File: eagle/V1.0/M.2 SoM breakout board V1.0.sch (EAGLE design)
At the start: 121 parts, among them J1 3-PIN SMD, J11 WAFER-HY2.0-4PWB, J18 PARTICLE-STUDIOS_M_SERIES_M.2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, J2 DCJ0202, J21 SIP-2, J3 SPARK_CON_30X2_SMD, J5 SCREW-HOLE-3.7, J6 M.2-SOM-BREAKOUT-BOARD-V0.3_M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, J7 SCREW-HOLE-3.7, Q1 DNP/L2N7002, Q2 SI2333DS, Q3 SI2333DS, Q4 SI2333DS, Q5 SI2333DS, U1 XC8107, X1 BU-SMA-G, X2 BU-SMA-G, X3 BU-SMA-G, X4 S8111-46R, X5 S8111-46R, X6 S8111-46R

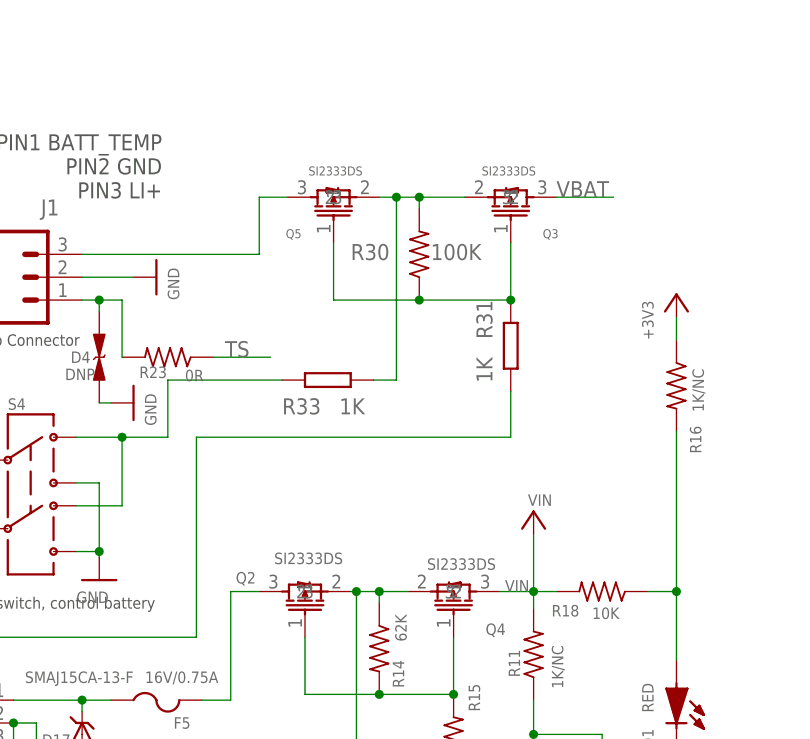
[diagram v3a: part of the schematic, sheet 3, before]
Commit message: Move Q2 position.
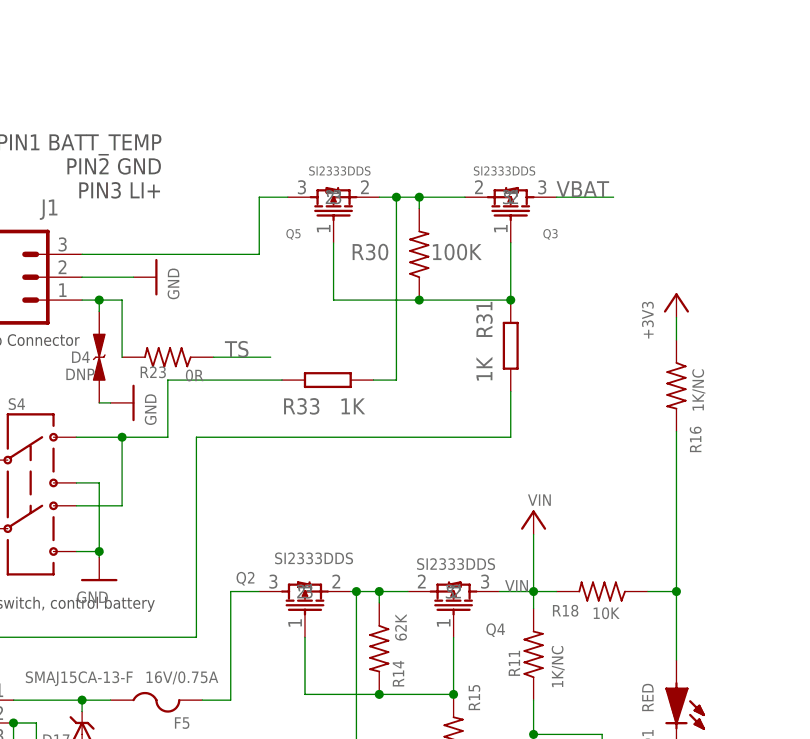
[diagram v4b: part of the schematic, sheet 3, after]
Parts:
- Q2, Q3, Q4, Q5: value SI2333DS -> SI2333DDS
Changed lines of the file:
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@@
 <part name="GND35" library="supply1" library_urn="urn:adsk.eagle:library:371" deviceset="GND" device=""/>
 <part name="S1" library="SparkFun-Retired" deviceset="SWITCH-DPDT" device=""/>
-<part name="Q4" library="RedBear" deviceset="PMOS" device="" value="SI2333DS"/>
+<part name="Q4" library="RedBear" deviceset="PMOS" device="" value="SI2333DDS"/>
 <part name="GND6" library="supply1" library_urn="urn:adsk.eagle:library:371" deviceset="GND" device=""/>
 <part name="R15" library="Particle" deviceset="R-US_" device="" value="36K"/>
@@
 <part name="J21" library="particle SZ" library_urn="urn:adsk.eagle:library:21650216" deviceset="SIP-2" device="" package3d_urn="urn:adsk.eagle:package:21650858/5"/>
 <part name="R30" library="particle-studios" library_urn="urn:adsk.eagle:library:10700396" deviceset="RES_" device="0603" package3d_urn="urn:adsk.eagle:package:10700443/4" technology="100K_" value="100K"/>
-<part name="Q3" library="RedBear" deviceset="PMOS" device="" value="SI2333DS"/>
-<part name="Q5" library="RedBear" deviceset="PMOS" device="" value="SI2333DS"/>
+<part name="Q3" library="RedBear" deviceset="PMOS" device="" value="SI2333DDS"/>
+<part name="Q5" library="RedBear" deviceset="PMOS" device="" value="SI2333DDS"/>
 <part name="R31" library="RedBear" deviceset="RES" device="0402S" value="1K"/>
 <part name="LED3" library="particle SZ" deviceset="LED" device="" value="yellow"/>
@@
 <part name="GND21" library="supply1" library_urn="urn:adsk.eagle:library:371" deviceset="GND" device=""/>
 <part name="D4" library="particle SZ" deviceset="ESD" device="" value="DNP"/>
-<part name="Q2" library="RedBear" deviceset="PMOS" device="" value="SI2333DS"/>
+<part name="Q2" library="RedBear" deviceset="PMOS" device="" value="SI2333DDS"/>
 <part name="R32" library="Particle" deviceset="R-US_" device="" value="1K"/>
 <part name="+3V3" library="supply1" library_urn="urn:adsk.eagle:library:371" deviceset="+3V3" device="" value="VIN"/>

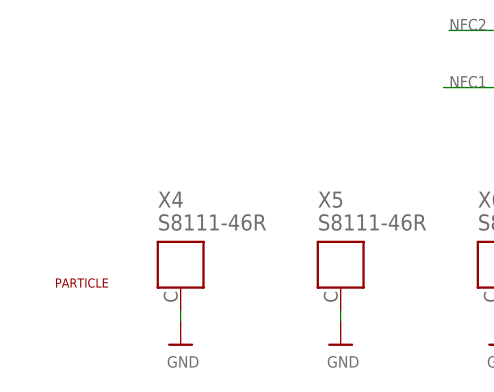
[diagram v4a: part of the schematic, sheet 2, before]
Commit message: updated label text and logo on the bottom
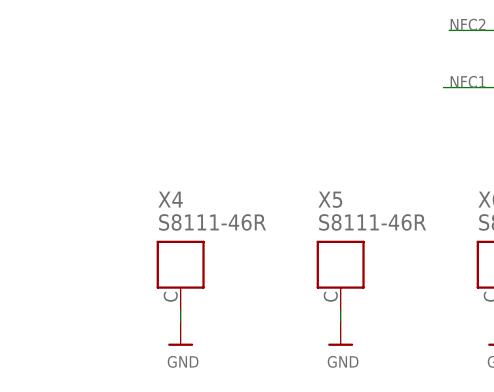
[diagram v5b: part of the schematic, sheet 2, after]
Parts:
- removed U$6: PARTICLE-LOGO, particle SZ:PARTICLE-LOGO
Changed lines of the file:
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@@
 <drawing>
 <settings>
-<setting alwaysvectorfont="no"/>
+<setting alwaysvectorfont="yes"/>
 <setting verticaltext="up"/>
 </settings>
@@
 <part name="R19" library="Particle" deviceset="R-US_" device="" value="1K"/>
 <part name="R20" library="Particle" deviceset="R-US_" device="" value="1K"/>
-<part name="U$6" library="particle SZ" deviceset="PARTICLE-LOGO" device=""/>
 <part name="NFC" library="Particle" deviceset="IPEX-20279-001E" device="" value="UFL"/>
 <part name="R37" library="RedBear" deviceset="RES" device="0402S" value="ESD NC"/>
@@
 <attribute name="VALUE" x="113.03" y="37.338" size="1.27" layer="96"/>
 </instance>
-<instance part="U$6" gate="G$1" x="10.16" y="13.97" smashed="yes"/>
 <instance part="NFC" gate="G$1" x="72.39" y="40.005" smashed="yes" rot="MR0">
 <attribute name="VALUE" x="69.215" y="38.735" size="1.27" layer="96" rot="MR0"/>

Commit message: typo
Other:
- note added: "GPIO1 is used for controlling the power module EN_AUX which make load switch work"
- note removed: "GPIO1 is used for ctroling the power module EN_AUX which make load switch work"
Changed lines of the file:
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@@
 <drawing>
 <settings>
-<setting alwaysvectorfont="yes"/>
+<setting alwaysvectorfont="no"/>
 <setting verticaltext="up"/>
 </settings>
-<grid distance="0.025" unitdist="inch" unit="inch" style="lines" multiple="1" display="yes" altdistance="0.01" altunitdist="inch" altunit="inch"/>
+<grid distance="0.1" unitdist="inch" unit="inch" style="lines" multiple="1" display="no" altdistance="0.01" altunitdist="inch" altunit="inch"/>
 <layers>
 <layer number="1" name="Top" color="4" fill="1" visible="no" active="no"/>
@@
 <text x="238.76" y="63.5" size="1.27" layer="97">23 Reserve for reset
 power module</text>
-<text x="143.51" y="48.895" size="1.27" layer="97">GPIO1 is used for ctroling
+<text x="143.51" y="48.895" size="1.27" layer="97">GPIO1 is used for controlling
 the power module EN_AUX which
  make load switch work </text>

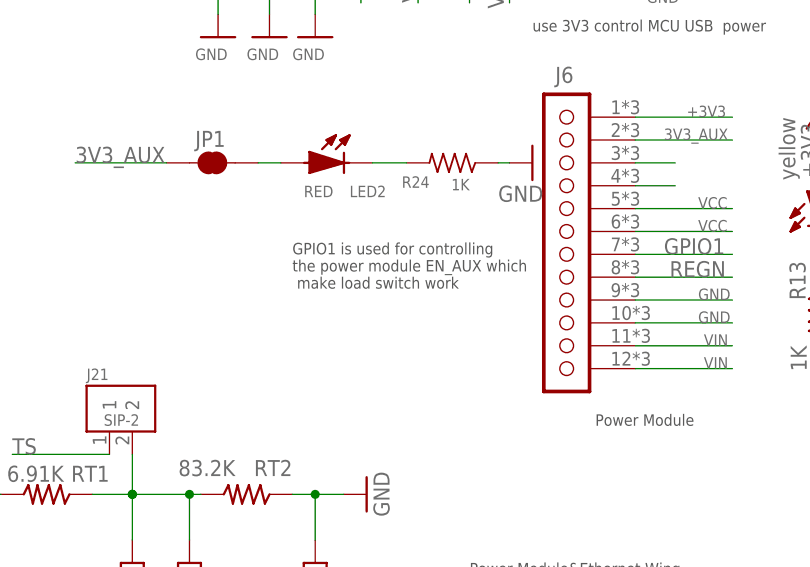
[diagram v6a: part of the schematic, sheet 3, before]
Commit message: Update M.2 SoM breakout board V1.0.sch
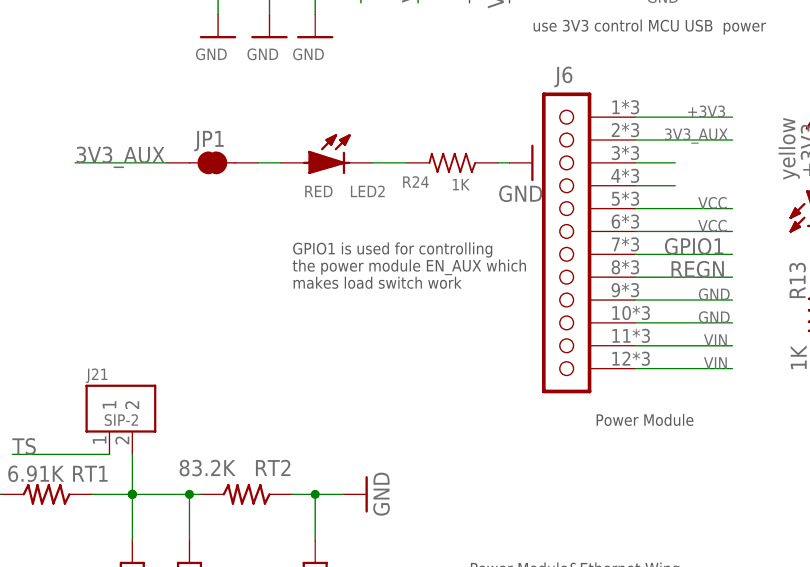
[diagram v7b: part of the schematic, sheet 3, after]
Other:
- note added: "GPIO1 is used for controlling the power module EN_AUX which makes load switch work"
- note removed: "GPIO1 is used for controlling the power module EN_AUX which make load switch work"
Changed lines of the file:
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@@
 <text x="143.51" y="48.895" size="1.27" layer="97">GPIO1 is used for controlling
 the power module EN_AUX which
- make load switch work </text>
+makes load switch work </text>
 </plain>
 <instances>
